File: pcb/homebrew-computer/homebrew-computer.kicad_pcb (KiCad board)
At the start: 4 copper layers, 93 parts, among them J1 Conn_01x02_Male, J2 Conn_01x02_Male, J3 Conn_02x03_Counter_Clockwise, J5 Conn_01x04_Male, J6 Conn_01x02, SW1 SW_Push, U1 AMS1117-3.3, U10 74LVC16374ADGG,112, U11 74LVC16374ADGG,112, U12 74LVC16374ADGG,112, U13 74LVC16374ADGG,112, U14 XC95144XL-10TQ100C, U15 74LVC16374ADGG,112, U16 DS1077LZ-60+, U17 74LVC1G157GC-Q100H, U18 74LVC1G14GW,125, U2 YC248, U3 YC248, U4 XC9572XL-10VQG44C, U5 SN74AVC16T245DGGR, U6 SN74AVC4T245PWR, U7 74LVC1G14GW,125, U8 XC9536XL-10VQG44C, U9 74LVC16374ADGG,112

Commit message: Keep working on the layout
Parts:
- added J4: Conn_02x20_Odd_Even, Connector_Molex:Molex_Pico-Clasp_203566-4007_2x20_P1.00mm_Horizontal, F.Cu at (125.0, 99.5)
- C13, C14, C15, C36, C37, C38, C39, C40, C41, C42, C47, C48, C49, C50, JP1, U14, U16, U17, U18, U2, U3, U8: moved to B.Cu
- J1, J2, J6: footprint Connector_Molex:Molex_PicoBlade_53048-0210_1x02_P1.25mm_Horizontal -> Connector_Molex:Molex_Pico-Clasp_202396-0207_1x02-1MP_P1.00mm_Horizontal
- J3: footprint Connector_PinHeader_2.54mm:PinHeader_2x03_P2.54mm_Vertical -> Connector_Molex:Molex_Pico-Clasp_202396-0607_1x06-1MP_P1.00mm_Horizontal
- J5: footprint Connector_PinHeader_2.54mm:PinHeader_2x02_P2.54mm_Vertical -> Connector_Molex:Molex_Pico-Clasp_202396-0607_1x06-1MP_P1.00mm_Horizontal
- R1, R2, R3, R4, R5, R6: footprint Resistor_SMD:R_0603_1608Metric -> Resistor_SMD:R_0402_1005Metric_Pad0.72x0.64mm_HandSolder
- R7: footprint Resistor_SMD:R_0603_1608Metric -> Resistor_SMD:R_0402_1005Metric_Pad0.72x0.64mm_HandSolder; moved to B.Cu
- moved J2 127.0 mm to (42.5, 123.0), turned to 270 degrees
- moved D2 125.9 mm to (48.0, 123.0), turned to 90 degrees
- moved R1 125.9 mm to (51.0, 123.0), turned to 270 degrees
- moved SW1 125.2 mm to (57.0, 123.0)
- moved R6 106.6 mm to (79.0, 66.0), turned to 90 degrees
- moved C3 103.7 mm to (81.0, 66.0), turned to 90 degrees
- moved U2 99.7 mm to (135.5, 169.5)
- moved R3 87.8 mm to (74.2, 83.4), turned to 270 degrees
- moved U3 87.7 mm to (135.5, 163.5)
- moved R4 86.1 mm to (86.0, 83.0), turned to 270 degrees
- moved D7 84.0 mm to (103.5, 79.0), turned to 90 degrees
- moved D3 82.9 mm to (100.5, 79.0), turned to 90 degrees
- moved C5 82.7 mm to (102.5, 107.3), turned to 135 degrees
- moved D5 82.4 mm to (98.5, 79.0), turned to 90 degrees
- moved D4 81.9 mm to (96.5, 79.0), turned to 90 degrees
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
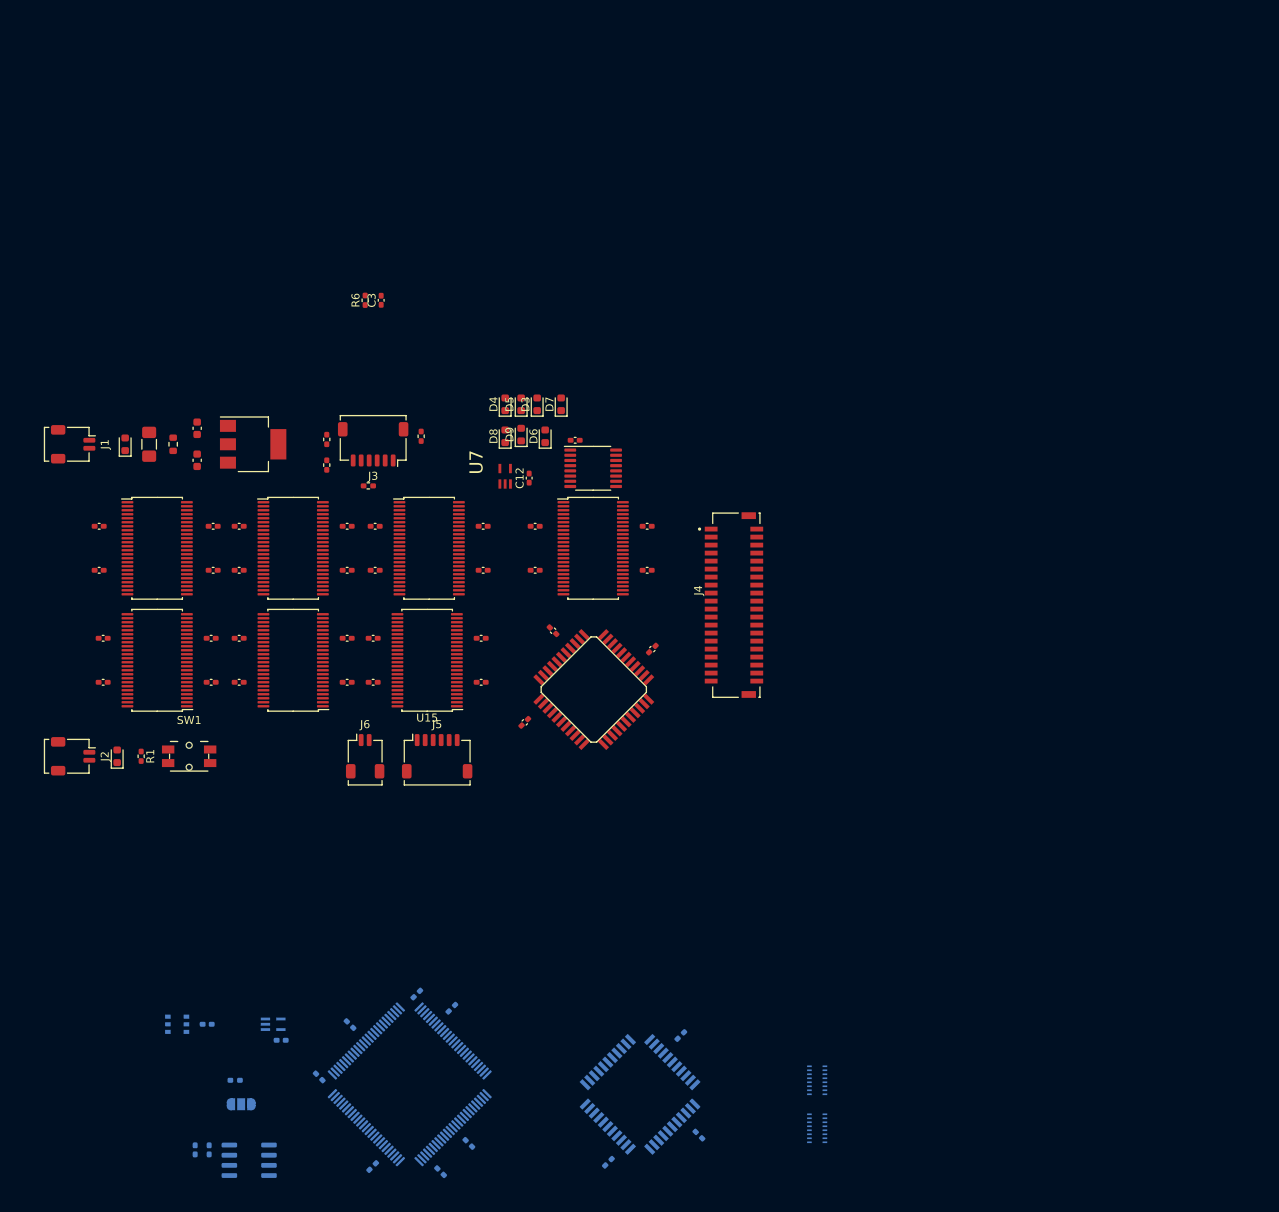
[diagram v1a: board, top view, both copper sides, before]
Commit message: Add the board outline
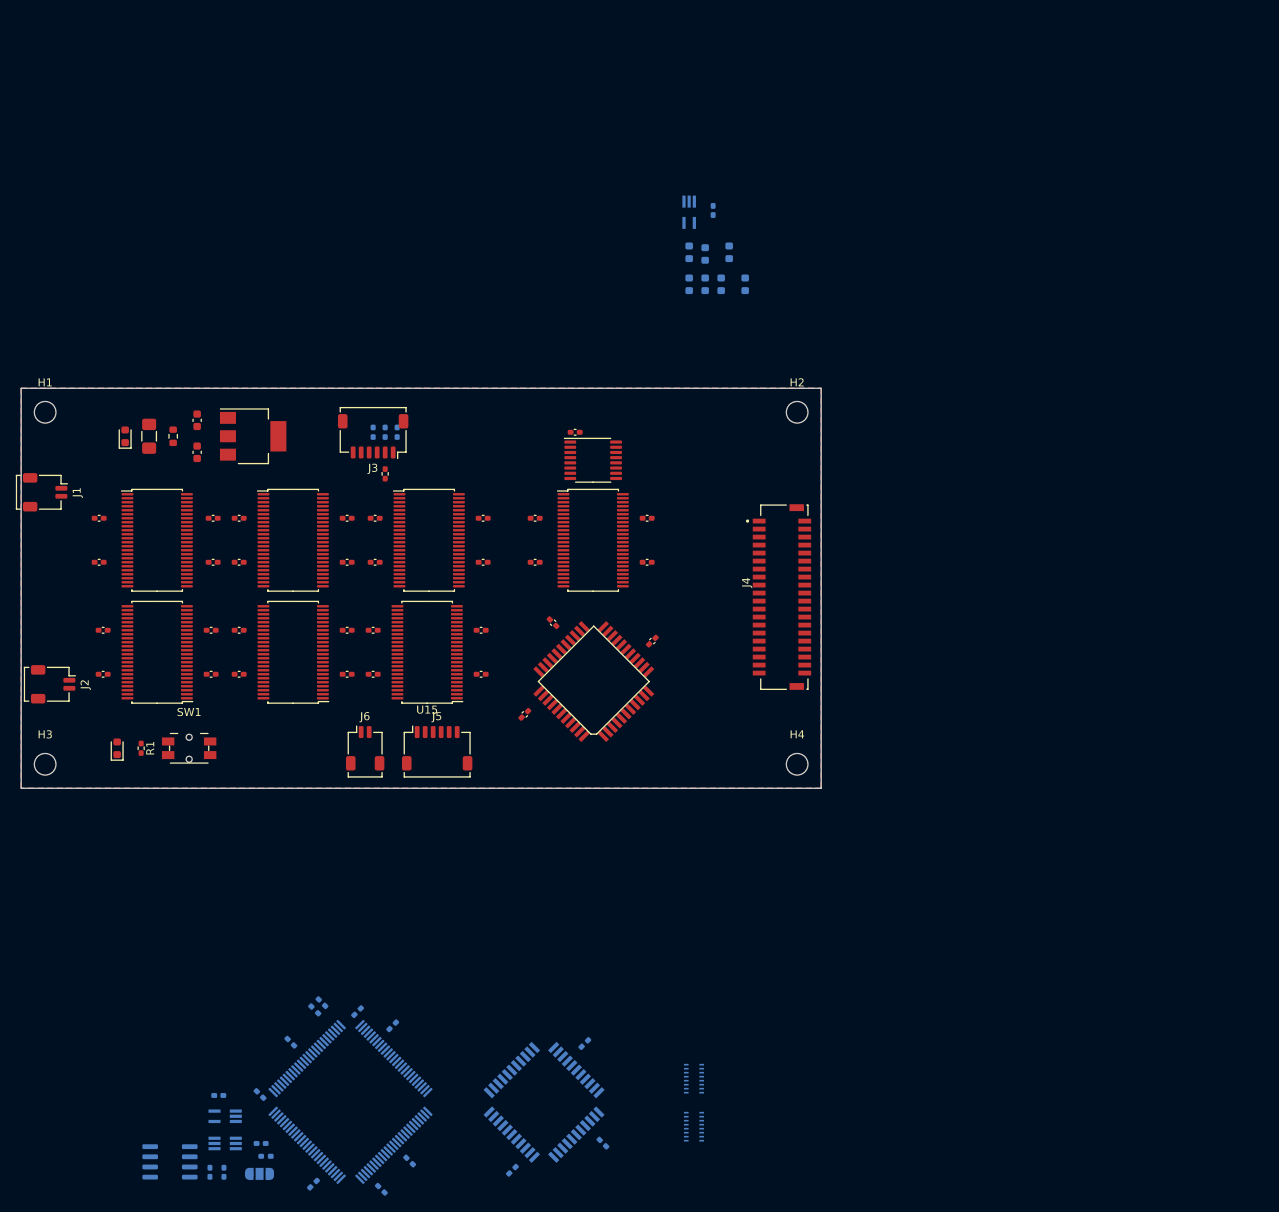
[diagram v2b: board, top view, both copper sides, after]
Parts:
- added H1: M3, MountingHole:MountingHole_2.7mm_M2.5, F.Cu at (39.0, 80.0)
- added H2: M3, MountingHole:MountingHole_2.7mm_M2.5, F.Cu at (133.0, 80.0)
- added H3: M3, MountingHole:MountingHole_2.7mm_M2.5, F.Cu at (39.0, 124.0)
- added H4: M3, MountingHole:MountingHole_2.7mm_M2.5, F.Cu at (133.0, 124.0)
- C12, C3, D3, D4, D5, D6, D7, D8, D9, R2, R3, R4, R6: moved to B.Cu
- U17: footprint Package_SO:TSOP-6_1.65x3.05mm_P0.95mm -> Package_TO_SOT_SMD:SOT-363_SC-70-6_Handsoldering
- U18: footprint Package_SO:TSSOP-5 -> Package_TO_SOT_SMD:SOT-353_SC-70-5_Handsoldering
- U7: footprint Package_SO:TSSOP-5 -> Package_TO_SOT_SMD:SOT-353_SC-70-5_Handsoldering; moved to B.Cu
- moved R6 88.9 mm to (72.7, 154.7), turned to 135 degrees
- moved C3 88.1 mm to (73.6, 153.8), turned to 315 degrees
- moved C12 40.6 mm to (122.5, 54.8), turned to 270 degrees
- moved U7 40.2 mm to (119.5, 55.0), turned to 270 degrees
- moved D6 32.5 mm to (124.5, 60.0), turned to 270 degrees
- moved D8 32.5 mm to (119.5, 60.0), turned to 270 degrees
- moved D9 32.2 mm to (121.5, 60.2), turned to 270 degrees
- moved D3 27.5 mm to (123.5, 64.0), turned to 270 degrees
- moved D4 27.5 mm to (119.5, 64.0), turned to 270 degrees
- moved D5 27.5 mm to (121.5, 64.0), turned to 270 degrees
- moved D7 27.5 mm to (126.5, 64.0), turned to 270 degrees
- moved C49 16.4 mm to (66.0, 171.4)
- moved U17 16.1 mm to (61.5, 171.4)
- moved U2 15.4 mm to (120.1, 169.3)
- moved U3 15.4 mm to (120.1, 163.3)
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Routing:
- added copper zone on In2.Cu, net +3V3
- added copper zone on B.Cu, net GND
- added copper zone on F.Cu, net GND
- added copper zone on In1.Cu, net GND
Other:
- board outline added: 100 x 50 mm

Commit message: Keep working on the layout
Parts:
- added D10: LED_Small, LED_SMD:LED_0805_2012Metric, F.Cu at (61.0, 81.0)
- added R8: 470, Resistor_SMD:R_0402_1005Metric_Pad0.72x0.64mm_HandSolder, B.Cu at (61.4, 81.0)
- C10, C18, C19, C22, C23: moved to B.Cu
- D1: footprint Diode_SMD:D_0603_1608Metric -> Diode_SMD:D_0603_1608Metric_Pad1.05x0.95mm_HandSolder
- D2, D3, D4, D5, D6, D7, D8, D9: footprint Diode_SMD:D_0603_1608Metric -> Diode_SMD:D_0402_1005Metric_Pad0.77x0.64mm_HandSolder
- J5: footprint Connector_Molex:Molex_Pico-Clasp_202396-0607_1x06-1MP_P1.00mm_Horizontal -> Connector_Molex:Molex_Pico-Clasp_202396-0407_1x04-1MP_P1.00mm_Horizontal
- JP1: value Jumper_NC_Dual -> Jumper_NC_Small; footprint Jumper:SolderJumper-3_P1.3mm_Open_RoundedPad1.0x1.5mm -> Jumper:SolderJumper-2_P1.3mm_Open_RoundedPad1.0x1.5mm
- SW1: footprint Button_Switch_SMD:Panasonic_EVQPUL_EVQPUC -> Button_Switch_SMD:Panasonic_EVQPUJ_EVQPUA
- U1: value AMS1117-3.3 -> TLV73333PDBV; footprint Package_TO_SOT_SMD:SOT-223-3_TabPin2 -> Package_TO_SOT_SMD:SOT-23-5
- U17: footprint Package_TO_SOT_SMD:SOT-363_SC-70-6_Handsoldering -> Package_TO_SOT_SMD:SOT-363_SC-70-6
- U18, U7: footprint Package_TO_SOT_SMD:SOT-353_SC-70-5_Handsoldering -> Package_TO_SOT_SMD:SOT-353_SC-70-5
- moved C14 76.1 mm to (117.1, 95.7), turned to 45 degrees
- moved JP1 72.0 mm to (40.0, 108.0), turned to 0 degrees
- moved C15 71.6 mm to (120.4, 107.0), turned to 315 degrees
- moved U8 65.1 mm to (112.0, 102.0), turned to 135 degrees
- moved C3 64.9 mm to (82.4, 89.5)
- moved C37 64.9 mm to (86.9, 90.6)
- moved C38 64.9 mm to (78.5, 94.4)
- moved C39 64.9 mm to (93.4, 109.3)
- moved C41 64.9 mm to (74.7, 101.0)
- moved C36 64.9 mm to (91.2, 92.4)
- moved C40 64.9 mm to (89.8, 112.8)
- moved C42 64.9 mm to (81.3, 112.2)
- moved R6 64.9 mm to (81.5, 90.4)
- moved U14 64.9 mm to (86.0, 101.9)
- moved C13 61.0 mm to (104.6, 97.9), turned to 135 degrees
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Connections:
- D4 pad 1: +3V3 -> Net-(D4-Pad1)
- D6 pad 1: +3V3 -> Net-(D4-Pad1)
- J4 pad 1: GND -> /IO/IO1
- J4 pad 10: /IO/IO13 -> /IO/INT2
- J4 pad 11: /IO/IO4 -> GND
- J4 pad 12: /IO/IO14 -> GND
- J4 pad 13: GND -> /IO/IO5
- J4 pad 14: GND -> /RST_INT
- J4 pad 15: /IO/IO5 -> /IO/IO6
- J4 pad 16: /IO/IO11 -> /RESET
- J4 pad 17: /IO/IO6 -> GND
- J4 pad 18: /IO/IO12 -> GND
- J4 pad 19: GND -> /IO/IO7
- J4 pad 2: GND -> /INT
- J4 pad 20: GND -> /IO_ADDR_IN
- J4 pad 21: /IO/IO7 -> /IO/IO8
- J4 pad 22: /IO/IO9 -> /IO_OUT
- J4 pad 23: /IO/IO8 -> GND
- J4 pad 24: /IO/IO10 -> GND
- J4 pad 25: /RESET -> /IO/IO9
- J4 pad 26: GND -> /IO_IN
- J4 pad 27: /INT -> /IO/IO10
- J4 pad 28: /IO_ADDR_IN -> /IO_OUTB
- J4 pad 29: /IO/INT0 -> GND
- J4 pad 3: /IO/IO1 -> /IO/IO2
- J4 pad 30: /IO_OUT -> GND
- J4 pad 31: GND -> /IO/IO11
- J4 pad 32: GND -> /IO_INB
- J4 pad 33: /IO/INT1 -> /IO/IO12
- J4 pad 34: /IO_IN -> /PERIPH_MEM_SPACE
- J4 pad 35: /IO/INT2 -> GND
- J4 pad 36: /IO_OUTB -> GND
- J4 pad 37: GND -> /IO/IO13
- J4 pad 38: /IO_INB -> /IO/IO15
- J4 pad 39: /RST_INT -> /IO/IO14
- J4 pad 4: /IO/IO15 -> /IO/INT0
- J4 pad 40: /PERIPH_MEM_SPACE -> /IO/IO16
- J4 pad 5: /IO/IO2 -> GND
- J4 pad 6: /IO/IO16 -> GND
- J4 pad 7: GND -> /IO/IO3
- J4 pad 8: GND -> /IO/INT1
- J4 pad 9: /IO/IO3 -> /IO/IO4
- JP1 pad 1: GND -> EXT_CLK_SELECT
- JP1 pad 2: EXT_CLK_SELECT -> +3V3
- U1 pad 1: GND -> Net-(C1-Pad1)
- U1 pad 2: +3V3 -> GND
- U2 pad 1: GND -> BUS8
- U2 pad 10: BUS2 -> GND
- U2 pad 11: BUS3 -> GND
- U2 pad 12: BUS4 -> GND
- U2 pad 13: BUS5 -> GND
- U2 pad 14: BUS6 -> GND
- U2 pad 15: BUS7 -> GND
- U2 pad 16: BUS8 -> GND
- U2 pad 2: GND -> BUS7
- U2 pad 3: GND -> BUS6
- U2 pad 4: GND -> BUS5
- U2 pad 5: GND -> BUS4
- U2 pad 6: GND -> BUS3
- U2 pad 7: GND -> BUS2
- U2 pad 8: GND -> BUS1
- U2 pad 9: BUS1 -> GND
- U3 pad 1: GND -> BUS16
- U3 pad 10: BUS10 -> GND
- U3 pad 11: BUS11 -> GND
- U3 pad 12: BUS12 -> GND
- U3 pad 13: BUS13 -> GND
- U3 pad 14: BUS14 -> GND
- U3 pad 15: BUS15 -> GND
- U3 pad 16: BUS16 -> GND
- U3 pad 2: GND -> BUS15
- U3 pad 3: GND -> BUS14
- U3 pad 4: GND -> BUS13
- U3 pad 5: GND -> BUS12
- U3 pad 6: GND -> BUS11
- U3 pad 7: GND -> BUS10
- U3 pad 8: GND -> BUS9
- U3 pad 9: BUS9 -> GND
- U4 pad 1: /OP_IN -> BUS10
- U4 pad 19: BUS15 -> Net-(U4-Pad19)
- U4 pad 2: /OP1 -> BUS11
- U4 pad 20: BUS14 -> Net-(U4-Pad20)
- U4 pad 21: BUS13 -> Net-(U4-Pad21)
- U4 pad 22: BUS12 -> Net-(U4-Pad22)
- U4 pad 23: BUS11 -> /OP4
- U4 pad 27: BUS10 -> /OP3
- U4 pad 28: BUS9 -> /OP2
- U4 pad 29: BUS8 -> /OP1
- U4 pad 3: /OP2 -> BUS12
- U4 pad 30: BUS7 -> /OP_IN
- U4 pad 31: BUS6 -> /B_IN
- U4 pad 32: BUS5 -> /A_IN
- U4 pad 34: BUS4 -> /ALU_OUT_I
- U4 pad 36: /ALU_OUT_I -> BUS1
- U4 pad 37: BUS3 -> BUS2
- U4 pad 38: BUS2 -> BUS3
- U4 pad 39: BUS1 -> BUS4
- U4 pad 40: BUS16 -> BUS5
- U4 pad 41: Net-(U4-Pad41) -> BUS6
- U4 pad 42: Net-(U4-Pad42) -> BUS7
- U4 pad 43: /A_IN -> BUS8
- U4 pad 44: /B_IN -> BUS9
- U4 pad 5: /OP3 -> BUS13
- U4 pad 6: /OP4 -> BUS14
- U4 pad 7: Net-(U4-Pad7) -> BUS15
- U4 pad 8: Net-(U4-Pad8) -> BUS16
- U5 pad 1: +3V3 -> Net-(D4-Pad1)
- U5 pad 24: +3V3 -> Net-(D4-Pad1)
- U8 pad 1: Net-(U8-Pad1) -> BUS10
- U8 pad 19: BUS15 -> Net-(U8-Pad19)
- U8 pad 2: Net-(U8-Pad2) -> BUS11
- U8 pad 20: BUS14 -> Net-(U8-Pad20)
- U8 pad 21: BUS13 -> Net-(U8-Pad21)
- U8 pad 22: BUS12 -> Net-(U8-Pad22)
- U8 pad 23: BUS11 -> Net-(U8-Pad23)
- U8 pad 27: BUS10 -> /PC_IN
- U8 pad 28: BUS9 -> /PC_COUNT
- U8 pad 29: BUS8 -> Net-(U8-Pad29)
- U8 pad 3: Net-(U8-Pad3) -> BUS12
- U8 pad 30: BUS7 -> Net-(U8-Pad30)
- U8 pad 31: BUS6 -> Net-(U8-Pad31)
- U8 pad 32: BUS5 -> Net-(U8-Pad32)
- U8 pad 34: BUS4 -> /PC_OUT_I
- U8 pad 36: /PC_OUT_I -> BUS1
- U8 pad 37: BUS3 -> BUS2
- U8 pad 38: BUS2 -> BUS3
- U8 pad 39: BUS1 -> BUS4
- U8 pad 40: BUS16 -> BUS5
- U8 pad 41: Net-(U8-Pad41) -> BUS6
- U8 pad 42: Net-(U8-Pad42) -> BUS7
- U8 pad 43: /PC_COUNT -> BUS8
- U8 pad 44: /PC_IN -> BUS9
- U8 pad 5: Net-(U8-Pad5) -> BUS13
- U8 pad 6: Net-(U8-Pad6) -> BUS14
- U8 pad 7: Net-(U8-Pad7) -> BUS15
- U8 pad 8: Net-(U8-Pad8) -> BUS16
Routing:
- net BUS1: track 0.00 -> 149.4 mm, vias 0 -> 1
- net BUS2: track 0.00 -> 146.9 mm, vias 0 -> 1
- net BUS3: track 0.00 -> 142.9 mm, vias 0 -> 1
- net BUS4: track 0.00 -> 140.4 mm, vias 0 -> 1
- net BUS5: track 0.00 -> 136.5 mm, vias 0 -> 1
- net BUS6: track 0.00 -> 134.2 mm, vias 0 -> 1
- net BUS7: track 0.00 -> 130.4 mm, vias 0 -> 1
- net BUS8: track 0.00 -> 128.7 mm, vias 0 -> 1
- net BUS9: track 0.00 -> 125.2 mm, vias 0 -> 1
- net BUS10: track 0.00 -> 122.2 mm, vias 0 -> 1
- net BUS11: track 0.00 -> 120.0 mm, vias 0 -> 1
- net BUS12: track 0.00 -> 118.6 mm, vias 0 -> 1
- net BUS13: track 0.00 -> 117.0 mm, vias 0 -> 1
- net BUS14: track 0.00 -> 115.6 mm, vias 0 -> 1
- net BUS15: track 0.00 -> 113.0 mm, vias 0 -> 1
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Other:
- net class Default: clearance 0.2 -> 0.127; trace_width 0.25 -> 0.127; via_dia 0.8 -> 0.45; via_drill 0.4 -> 0.2
- rule trace_clearance: 0.2 -> 0.127
- rule trace_min: 0.2 -> 0.127
- rule via_min_drill: 0.3 -> 0.2
- rule via_min_size: 0.4 -> 0.45

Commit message: Keep working on the layout
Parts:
- D2, R1: moved to B.Cu
- moved JP1 22.3 mm to (59.4, 119.0), turned to 270 degrees
- moved D2 0.90 mm to (49.9, 122.7)
- moved C49 0.81 mm to (64.5, 119.9), turned to 180 degrees
- moved R7 0.39 mm to (64.8, 117.8)
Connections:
- J4 pad 10: /IO/INT2 -> /IO/INT0
- J4 pad 4: /IO/INT0 -> /IO/INT2
- U4 pad 12: Net-(U4-Pad12) -> /FLAG_ZERO
- U4 pad 13: /FLAG_ZERO -> /FLAG_NEG
- U4 pad 14: /FLAG_NEG -> /FLAG_CARRY
- U4 pad 16: /FLAG_CARRY -> /FLAG_OVERFLOW
- U4 pad 18: /FLAG_OVERFLOW -> /OP_IN
- U4 pad 19: Net-(U4-Pad19) -> /OP4
- U4 pad 20: Net-(U4-Pad20) -> /OP3
- U4 pad 21: Net-(U4-Pad21) -> /OP2
- U4 pad 22: Net-(U4-Pad22) -> /OP1
- U4 pad 23: /OP4 -> /B_IN
- U4 pad 27: /OP3 -> /A_IN
- U4 pad 28: /OP2 -> Net-(U4-Pad28)
- U4 pad 29: /OP1 -> Net-(U4-Pad29)
- U4 pad 30: /OP_IN -> Net-(U4-Pad30)
- U4 pad 31: /B_IN -> Net-(U4-Pad31)
- U4 pad 32: /A_IN -> Net-(U4-Pad32)
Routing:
- net EXT_CLK: track 0.00 -> 38.3 mm, vias 0 -> 1
- net /IO/INT0: track 0.00 -> 25.0 mm
- net /IO/INT1: track 0.00 -> 24.7 mm
- net /IO/INT2: track 0.00 -> 23.6 mm
- net /Control Logic/IR16: track 0.00 -> 17.2 mm, vias 0 -> 1
- net /Control Logic/IR15: track 0.00 -> 16.2 mm, vias 0 -> 1
- net /Control Logic/IR14: track 0.00 -> 14.7 mm, vias 0 -> 1
- net /Control Logic/IR13: track 0.00 -> 13.9 mm, vias 0 -> 1
- net /Control Logic/IR12: track 0.00 -> 12.7 mm, vias 0 -> 1
- net /Control Logic/IR11: track 0.00 -> 11.9 mm, vias 0 -> 1
- net /RESET: track 0.00 -> 11.1 mm, vias 0 -> 1
- net Net-(D2-Pad2): track 0.00 -> 10.8 mm, vias 0 -> 1
- net /Control Logic/IR10: track 0.00 -> 10.6 mm, vias 0 -> 1
- net /Control Logic/IR9: track 0.00 -> 9.78 mm, vias 0 -> 1
- net BUS3: track 142.9 -> 152.6 mm, vias 1 -> 3
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
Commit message: Keep working on the layout
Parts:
- C40, C42: moved to F.Cu
- moved U13 36.8 mm to (60.5, 109.0), turned to 180 degrees
- moved U11 36.5 mm to (94.2, 95.0), turned to 0 degrees
- moved U10 17.0 mm to (77.5, 95.0)
- moved U12 17.0 mm to (60.5, 95.0)
- moved C42 6.40 mm to (85.9, 107.7), turned to 0 degrees
- moved C10 5.88 mm to (118.9, 92.2), turned to 0 degrees
- moved C40 4.69 mm to (85.9, 110.2), turned to 180 degrees
- moved C12 4.35 mm to (114.8, 92.4), turned to 180 degrees
- moved C15 1.26 mm to (120.3, 105.8)
- moved C13 0.78 mm to (105.0, 97.3)
- moved C14 0.74 mm to (116.6, 95.1)
- moved C32 0.55 mm to (101.8, 97.8)
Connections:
- U14 pad 1: /REG3_IN_L -> /Control Logic/IR8
- U14 pad 10: /REG3_IN_H -> /Control Logic/IR16
- U14 pad 11: /OP2 -> /REG3_IN_L
- U14 pad 12: /OP3 -> Net-(U14-Pad12)
- U14 pad 13: /OP4 -> Net-(U14-Pad13)
- U14 pad 15: /FLAG_NEG -> Net-(U14-Pad15)
- U14 pad 16: /FLAG_ZERO -> Net-(U14-Pad16)
- U14 pad 17: /FLAG_CARRY -> Net-(U14-Pad17)
- U14 pad 18: /FLAG_OVERFLOW -> Net-(U14-Pad18)
- U14 pad 19: /REG1_OUT_L_I -> Net-(U14-Pad19)
- U14 pad 2: /SP_OUT_I -> /Control Logic/IR9
- U14 pad 20: /REG1_OUT_H_I -> Net-(U14-Pad20)
- U14 pad 23: /REG1_IN_H -> Net-(U14-Pad23)
- U14 pad 24: /REG1_IN_L -> Net-(U14-Pad24)
- U14 pad 25: /REG2_OUT_L_I -> Net-(U14-Pad25)
- U14 pad 29: /REG2_IN_H -> /REG1_IN_H
- U14 pad 3: /SP_IN -> /Control Logic/IR10
- U14 pad 30: /REG2_IN_L -> /BP_OUT_I
- U14 pad 32: /REG3_OUT_L_I -> /BP_IN
- U14 pad 33: /REG3_OUT_H_I -> /SP_OUT_I
- U14 pad 34: Net-(U14-Pad34) -> /SP_IN
- U14 pad 35: /Control Logic/IR11 -> Net-(U14-Pad35)
- U14 pad 36: /Control Logic/IR12 -> Net-(U14-Pad36)
- U14 pad 37: /Control Logic/IR13 -> Net-(U14-Pad37)
- U14 pad 39: /Control Logic/IR14 -> Net-(U14-Pad39)
- U14 pad 4: /BP_OUT_I -> /Control Logic/IR11
- U14 pad 40: /Control Logic/IR15 -> Net-(U14-Pad40)
- U14 pad 41: /Control Logic/IR16 -> /REG3_IN_H
- U14 pad 42: /A_IN -> Net-(U14-Pad42)
- U14 pad 43: /B_IN -> Net-(U14-Pad43)
- U14 pad 46: /OP_IN -> Net-(U14-Pad46)
- U14 pad 49: /OP1 -> Net-(U14-Pad49)
- U14 pad 6: /BP_IN -> /Control Logic/IR12
- U14 pad 61: /Control Logic/INSTR_IN -> Net-(U14-Pad61)
- U14 pad 7: /PC_COUNT -> /Control Logic/IR13
- U14 pad 72: Net-(U14-Pad72) -> /PC_IN
- U14 pad 73: Net-(U14-Pad73) -> /PC_COUNT
- U14 pad 74: Net-(U14-Pad74) -> /PC_OUT_I
- U14 pad 76: Net-(U14-Pad76) -> /FLAG_ZERO
- U14 pad 77: Net-(U14-Pad77) -> /FLAG_NEG
- U14 pad 78: Net-(U14-Pad78) -> /FLAG_CARRY
- U14 pad 79: Net-(U14-Pad79) -> /FLAG_OVERFLOW
- U14 pad 8: /PC_IN -> /Control Logic/IR14
- U14 pad 80: Net-(U14-Pad80) -> /OP_IN
- U14 pad 81: Net-(U14-Pad81) -> /OP4
- U14 pad 82: Net-(U14-Pad82) -> /OP3
- U14 pad 85: Net-(U14-Pad85) -> /OP2
- U14 pad 86: Net-(U14-Pad86) -> /OP1
- U14 pad 87: /Control Logic/IR1 -> /B_IN
- U14 pad 89: /Control Logic/IR2 -> /A_IN
- U14 pad 9: /PC_OUT_I -> /Control Logic/IR15
- U14 pad 90: /Control Logic/IR3 -> /Control Logic/IR1
- U14 pad 91: /Control Logic/IR4 -> /Control Logic/IR2
- U14 pad 92: /Control Logic/IR5 -> /Control Logic/IR3
- U14 pad 93: /Control Logic/IR6 -> /Control Logic/IR4
- U14 pad 94: /Control Logic/IR7 -> /Control Logic/IR5
- U14 pad 95: /Control Logic/IR8 -> /Control Logic/IR6
- U14 pad 96: /Control Logic/IR9 -> /Control Logic/IR7
- U14 pad 97: /Control Logic/IR10 -> /Control Logic/INSTR_IN
- U8 pad 12: Net-(U8-Pad12) -> /PC_OUT_I
- U8 pad 13: Net-(U8-Pad13) -> /PC_COUNT
- U8 pad 14: Net-(U8-Pad14) -> /PC_IN
- U8 pad 27: /PC_IN -> Net-(U8-Pad27)
- U8 pad 28: /PC_COUNT -> Net-(U8-Pad28)
- U8 pad 34: /PC_OUT_I -> Net-(U8-Pad34)
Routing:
- net /A_IN: track 0.00 -> 30.8 mm, vias 0 -> 1
- net /B_IN: track 0.00 -> 26.2 mm, vias 0 -> 1
- net /SP_OUT_I: track 0.00 -> 24.1 mm
- net /BP_IN: track 0.00 -> 23.9 mm
- net /OP1: track 0.00 -> 23.2 mm, vias 0 -> 1
- net /OP2: track 0.00 -> 22.2 mm, vias 0 -> 1
- net /OP3: track 0.00 -> 20.8 mm, vias 0 -> 1
- net /OP4: track 0.00 -> 19.8 mm, vias 0 -> 1
- net /OP_IN: track 0.00 -> 18.8 mm, vias 0 -> 1
- net /FLAG_OVERFLOW: track 0.00 -> 16.7 mm, vias 0 -> 1
- net /SP_IN: track 0.00 -> 16.5 mm
- net /BP_OUT_I: track 0.00 -> 15.4 mm
- net /FLAG_CARRY: track 0.00 -> 15.1 mm, vias 0 -> 1
- net /FLAG_NEG: track 0.00 -> 14.1 mm, vias 0 -> 1
- net /Control Logic/IR16: track 17.2 -> 30.8 mm
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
